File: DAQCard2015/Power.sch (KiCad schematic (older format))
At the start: 19 parts, among them CON1 BARREL_JACK, SW1 DPDT, U20 LM1086, U21 LT1913

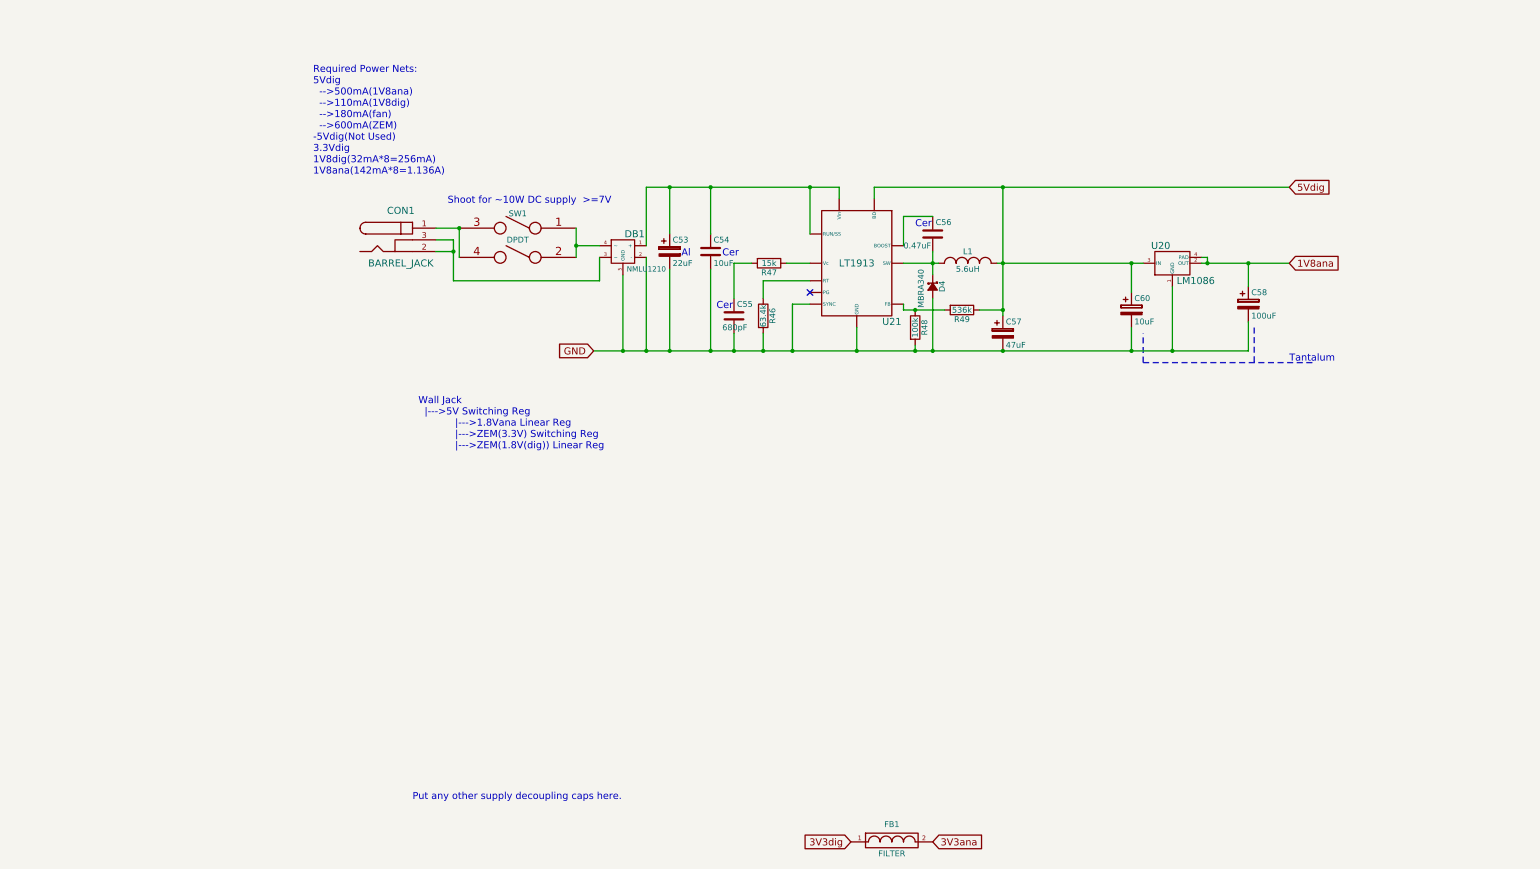
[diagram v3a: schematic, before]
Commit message: Update to DAQ Board including adding an JTAG header and hooking up external clock and trigger
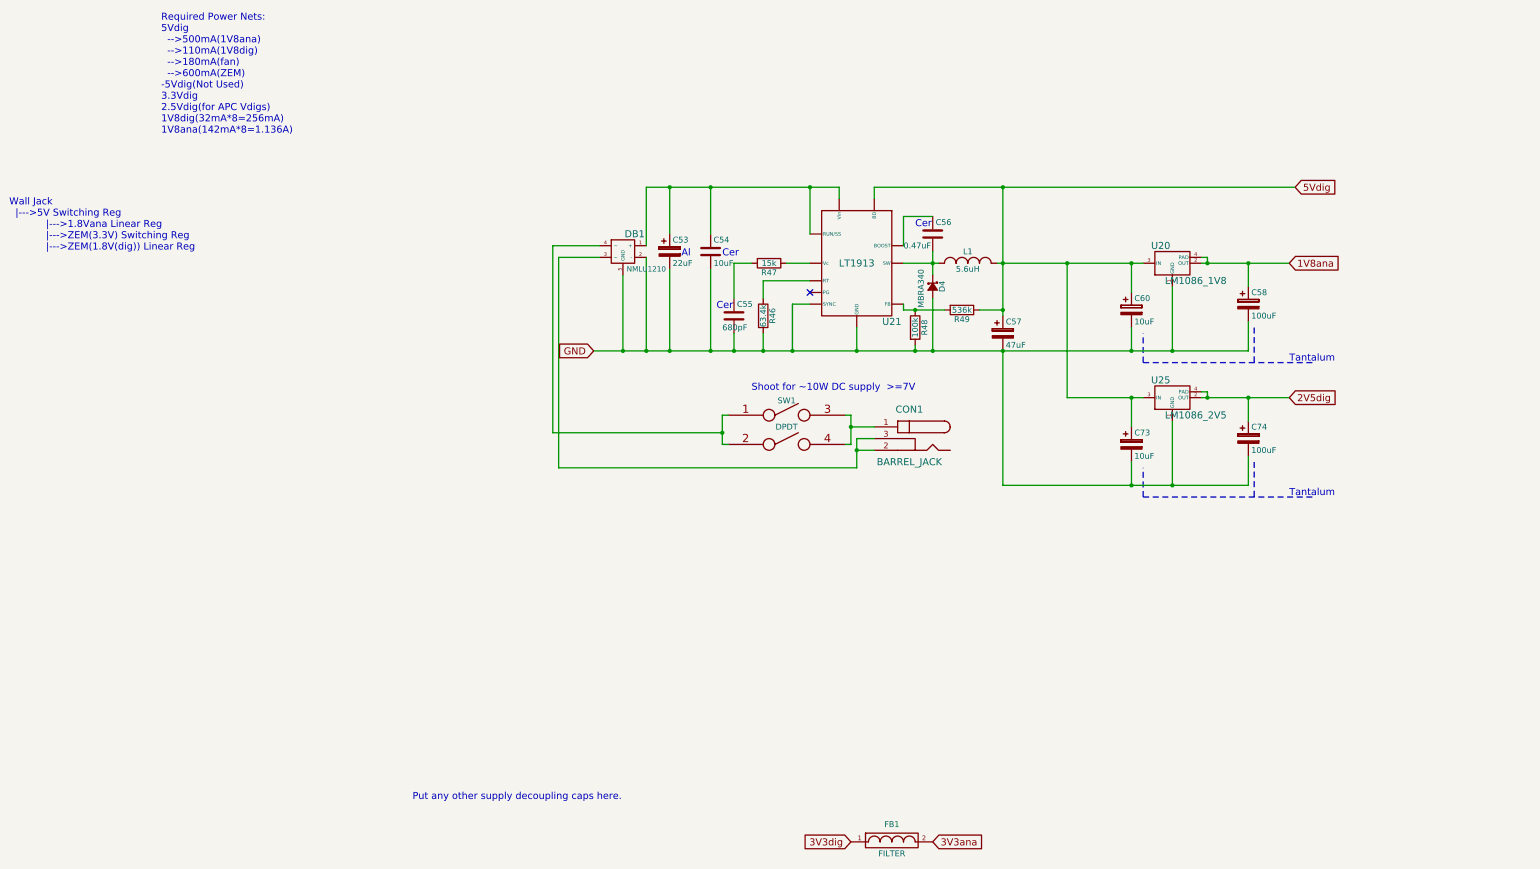
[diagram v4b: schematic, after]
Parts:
- added C73: 10uF, Capacitors_Tantalum_SMD:TantalC_SizeD_EIA-7343_Reflow, symbol CP
- added C74: 100uF, Capacitors_Tantalum_SMD:TantalC_SizeD_EIA-7343_Reflow, symbol CP
- added U25: LM1086_2V5, extras:TO-263-4, symbol LM1086
- U20: value LM1086 -> LM1086_1V8
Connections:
- net 5Vdig: now also C73.1, U25.3 (IN)
- net GND: now also C73.2, C74.2, U25.1 (GND)
- new net 2V5dig: C74.1, U25.2 (OUT), U25.4 (PAD)
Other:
- note added: "Required Power Nets:\n5Vdig\n -->500mA(1V8ana)\n -->110mA(1V8dig)\n -->180mA(fan)\n -->600mA(ZEM)\n-5Vdig(Not Used)\n3.3Vdig\n2.5Vdig(for APC Vdigs)\n1V8dig(32mA*8=256mA)\n1V8ana(142mA*8=1.136A)"
- note removed: "Required Power Nets:\n5Vdig\n -->500mA(1V8ana)\n -->110mA(1V8dig)\n -->180mA(fan)\n -->600mA(ZEM)\n-5Vdig(Not Used)\n3.3Vdig\n1V8dig(32mA*8=256mA)\n1V8ana(142mA*8=1.136A)"
- moved on the sheet: CON1, SW1
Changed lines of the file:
@@
 Comment4 ""
 $EndDescr
-Text Notes 700  1400 0    60   ~ 0
-Required Power Nets:\n5Vdig\n  -->500mA(1V8ana)\n  -->110mA(1V8dig)\n  -->180mA(fan)\n  -->600mA(ZEM)\n-5Vdig(Not Used)\n3.3Vdig\n1V8dig(32mA*8=256mA)\n1V8ana(142mA*8=1.136A)
+Text Notes -600 1050 0    60   ~ 0
+Required Power Nets:\n5Vdig\n  -->500mA(1V8ana)\n  -->110mA(1V8dig)\n  -->180mA(fan)\n  -->600mA(ZEM)\n-5Vdig(Not Used)\n3.3Vdig\n2.5Vdig(for APC Vdigs)\n1V8dig(32mA*8=256mA)\n1V8ana(142mA*8=1.136A)
 Text GLabel 9050 2150 2    60   Input ~ 0
 1V8ana
@@
 L BARREL_JACK CON1
 U 1 1 55CCF566
-P 1450 1950
-F 0 "CON1" H 1450 2200 60  0000 C CNN
-F 1 "BARREL_JACK" H 1450 1750 60  0000 C CNN
-F 2 "Connect:BARREL_JACK" H 1450 1950 60  0001 C CNN
-F 3 "" H 1450 1950 60  0000 C CNN
-	1    1450 1950
-	1    0    0    -1
+P 5800 3650
+F 0 "CON1" H 5800 3900 60  0000 C CNN
+F 1 "BARREL_JACK" H 5800 3450 60  0000 C CNN
+F 2 "Connect:BARREL_JACK" H 5800 3650 60  0001 C CNN
+F 3 "" H 5800 3650 60  0000 C CNN
+	1    5800 3650
+	-1   0    0    -1
 $EndComp
 Text GLabel 3100 2900 0    60   Input ~ 0
 GND
-Text Notes 1850 1650 0    60   ~ 0
+Text Notes 4450 3250 0    60   ~ 0
 Shoot for ~~10W DC supply  >=7V
 $Comp
@@
 P 8050 2350
 F 0 "U20" H 7950 2700 60  0000 C CNN
-F 1 "LM1086" H 8250 2400 60  0000 C CNN
+F 1 "LM1086_1V8" H 8250 2400 60  0000 C CNN
 F 2 "extras:TO-263-4" H 8050 2350 60  0001 C CNN
 F 3 "" H 8050 2350 60  0000 C CNN
@@
 	1    0    0    -1
 $EndComp
-Text GLabel 9050 1500 2    60   Input ~ 0
+Text GLabel 9100 1500 2    60   Input ~ 0
 5Vdig
-$Comp
-L DPDT SW1
-U 1 1 55F79633
-P 2450 1850
-F 0 "SW1" H 2450 1975 50  0000 C CNN
-F 1 "DPDT" H 2450 1750 50  0000 C CNN
-F 2 "extras:DFXX-XX-X-XX-A-X-XX" H 2450 1850 60  0001 C CNN
-F 3 "" H 2450 1850 60  0000 C CNN
-	1    2450 1850
-	-1   0    0    -1
-$EndComp
 $Comp
 L LT1913 U21
@@
 	1    0    0    -1
 $EndComp
-Text Notes 1600 3750 0    60   ~ 0
+Text Notes -1900 2050 0    60   ~ 0
 Wall Jack\n  |--->5V Switching Reg\n            |--->1.8Vana Linear Reg\n            |--->ZEM(3.3V) Switching Reg\n            |--->ZEM(1.8V(dig)) Linear Reg\n
 $Comp
@@
 Text Notes 5850 1850 0    60   ~ 0
 Cer
-Connection ~ 2950 2000
-Wire Wire Line
-	1950 1850 1950 2100
 Connection ~ 4950 1500
 Wire Wire Line
-	4950 1900 4950 1500
+	4950 1500 4950 1900
 Connection ~ 3350 2900
 Wire Wire Line
@@
 Connection ~ 3550 2900
 Wire Wire Line
-	8700 2350 8700 2150
+	8700 2150 8700 2350
 Connection ~ 6600 2900
 Connection ~ 6600 1500
@@
 Connection ~ 6600 2550
 Wire Wire Line
-	5500 1500 9050 1500
+	5500 1500 9100 1500
 Connection ~ 6000 2900
 Wire Wire Line
-	6000 2450 6000 2900
+	6000 2900 6000 2450
 Wire Wire Line
 	6600 2550 6400 2550
@@
 Connection ~ 4800 2900
 Wire Wire Line
-	4800 2500 4800 2900
-Wire Wire Line
-	4950 2500 4800 2500
+	4800 2900 4800 2500
+Wire Wire Line
+	4800 2500 4950 2500
 Connection ~ 4550 2900
 Wire Wire Line
-	4550 2750 4550 2900
+	4550 2900 4550 2750
 Wire Wire Line
 	4550 2300 4550 2450
@@
 Connection ~ 4300 2900
 Wire Wire Line
-	4300 2750 4300 2900
+	4300 2900 4300 2750
 Wire Wire Line
 	4300 2150 4300 2450
@@
 	6550 2150 7800 2150
 Wire Wire Line
-	3150 2300 3150 2100
-Wire Wire Line
-	1900 2300 3150 2300
+	2800 2100 3150 2100
+Wire Wire Line
+	2800 3900 5350 3900
 Wire Wire Line
 	3550 2000 3550 1500
@@
 	3550 2900 3550 2100
 Wire Wire Line
-	2950 2000 3150 2000
-Wire Wire Line
-	2950 1850 2950 2100
+	2750 2000 3150 2000
 Connection ~ 4100 1500
 Connection ~ 3750 1500
@@
 Wire Wire Line
 	3550 1500 5200 1500
-Wire Wire Line
-	1750 1850 1950 1850
-Connection ~ 1900 2050
-Wire Wire Line
-	1900 1950 1900 2300
-Wire Wire Line
-	1750 1950 1900 1950
-Wire Wire Line
-	1900 2050 1750 2050
-Connection ~ 1950 1850
+Connection ~ 5350 3750
+Wire Wire Line
+	5350 3900 5350 3650
+Wire Wire Line
+	5350 3650 5500 3650
+Wire Wire Line
+	5350 3750 5500 3750
 Wire Notes Line
 	8750 2700 8750 3000
@@
 $EndComp
 Wire Wire Line
-	7700 2700 7700 2900
+	7700 2900 7700 2700
 Connection ~ 7700 2900
 Wire Wire Line
@@
 	1    0    0    -1
 $EndComp
+Text GLabel 9050 3300 2    60   Input ~ 0
+2V5dig
+$Comp
+L LM1086 U25
+U 1 1 56067747
+P 8050 3500
+F 0 "U25" H 7950 3850 60  0000 C CNN
+F 1 "LM1086_2V5" H 8250 3550 60  0000 C CNN
+F 2 "extras:TO-263-4" H 8050 3500 60  0001 C CNN
+F 3 "" H 8050 3500 60  0000 C CNN
+	1    8050 3500
+	1    0    0    -1
+$EndComp
+Wire Wire Line
+	8700 3300 8700 3500
+Connection ~ 8050 4050
+Wire Wire Line
+	8700 4050 8700 3800
+Connection ~ 8700 3300
+Wire Wire Line
+	8050 4050 8050 3500
+Connection ~ 8350 3300
+Wire Wire Line
+	8300 3300 9050 3300
+Wire Wire Line
+	8350 3250 8350 3300
+Wire Wire Line
+	8300 3250 8350 3250
+Wire Notes Line
+	8750 3850 8750 4150
+Wire Notes Line
+	7800 4150 9250 4150
+Text Notes 9050 4150 0    60   ~ 0
+Tantalum
+$Comp
+L CP C74
+U 1 1 5606775A
+P 8700 3650
+F 0 "C74" H 8725 3750 50  0000 L CNN
+F 1 "100uF" H 8725 3550 50  0000 L CNN
+F 2 "Capacitors_Tantalum_SMD:TantalC_SizeD_EIA-7343_Reflow" H 8738 3500 30  0001 C CNN
+F 3 "" H 8700 3650 60  0000 C CNN
+	1    8700 3650
+	1    0    0    -1
+$EndComp
+$Comp
+L CP C73
+U 1 1 56067760
+P 7700 3700
+F 0 "C73" H 7725 3800 50  0000 L CNN
+F 1 "10uF" H 7725 3600 50  0000 L CNN
+F 2 "Capacitors_Tantalum_SMD:TantalC_SizeD_EIA-7343_Reflow" H 7738 3550 30  0001 C CNN
+F 3 "" H 7700 3700 60  0000 C CNN
+	1    7700 3700
+	1    0    0    -1
+$EndComp
+Wire Wire Line
+	7700 3850 7700 4050
+Connection ~ 7700 4050
+Wire Wire Line
+	7700 3550 7700 3300
+Connection ~ 7700 3300
+Wire Notes Line
+	7800 4150 7800 3900
+Wire Wire Line
+	6600 4050 8700 4050
+Wire Wire Line
+	7150 3300 7150 2150
+Connection ~ 7150 2150
+Wire Wire Line
+	7150 3300 7800 3300
+Wire Wire Line
+	6600 4050 6600 2900
+Wire Wire Line
+	4250 3450 4200 3450
+Wire Wire Line
+	4200 3450 4200 3700
+Wire Wire Line
+	4200 3700 4250 3700
+Wire Wire Line
+	2750 3600 4200 3600
+Connection ~ 4200 3600
+$Comp
+L DPDT SW1
+U 1 1 55F79633
+P 4750 3450
+F 0 "SW1" H 4750 3575 50  0000 C CNN
+F 1 "DPDT" H 4750 3350 50  0000 C CNN
+F 2 "extras:DFXX-XX-X-XX-A-X-XX" H 4750 3450 60  0001 C CNN
+F 3 "" H 4750 3450 60  0000 C CNN
+	1    4750 3450
+	1    0    0    -1
+$EndComp
+Wire Wire Line
+	5250 3700 5300 3700
+Wire Wire Line
+	5300 3700 5300 3450
+Wire Wire Line
+	5300 3450 5250 3450
+Wire Wire Line
+	5500 3550 5300 3550
+Connection ~ 5300 3550
+Wire Wire Line
+	2750 3600 2750 2000
+Wire Wire Line
+	2800 3900 2800 2100
 $EndSCHEMATC
